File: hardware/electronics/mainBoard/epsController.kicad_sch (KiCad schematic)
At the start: 33 parts, among them SW10 PTS810, SW9 PTS810, U19 STM32L052K8, U20 TCAN3403-Q1

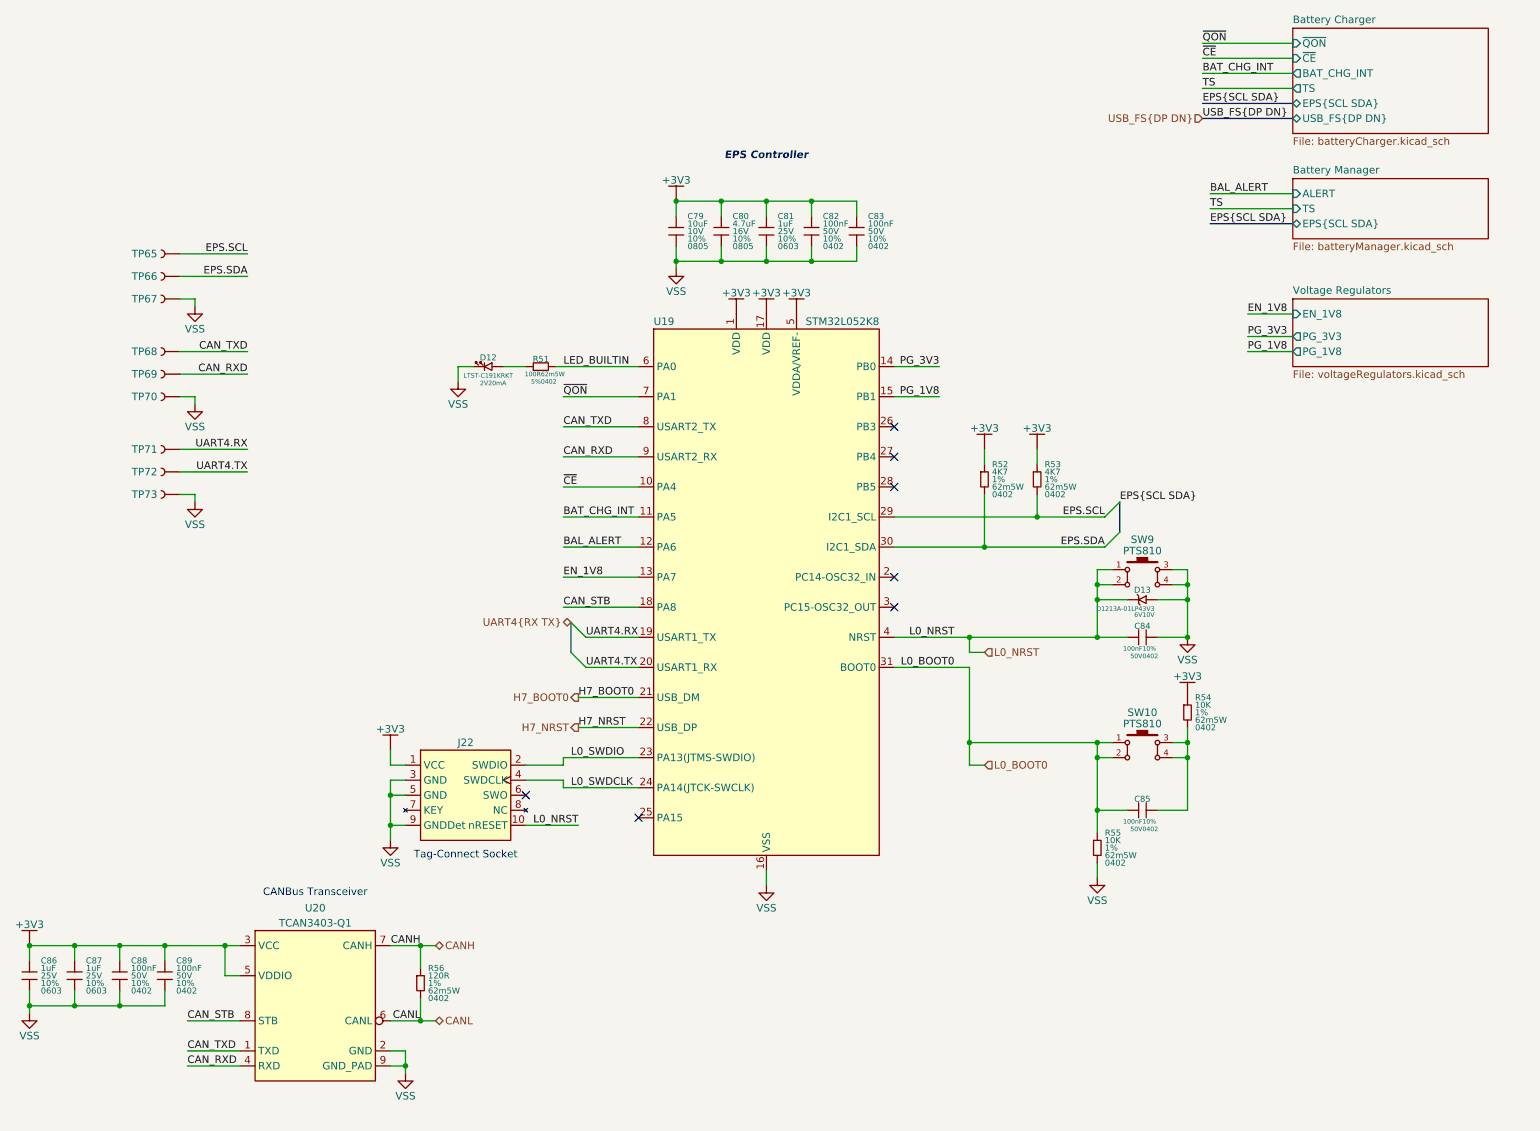
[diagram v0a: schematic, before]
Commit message: updated symbol refs
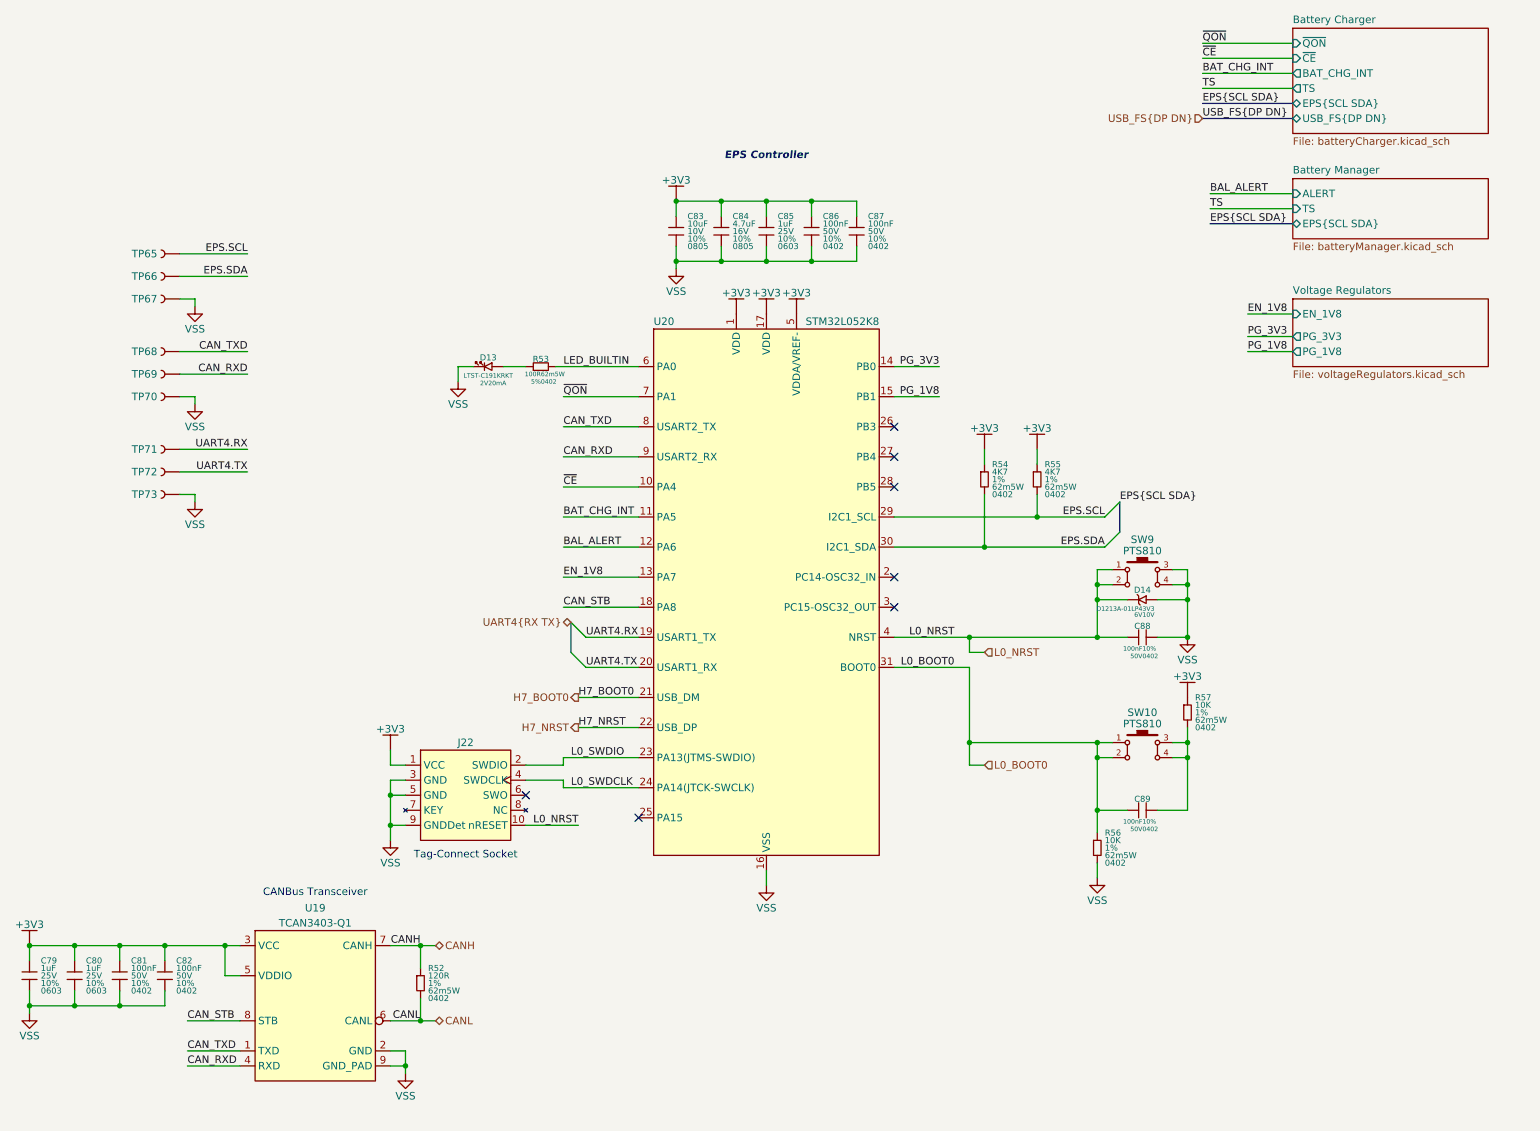
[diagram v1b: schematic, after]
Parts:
- renumbered C86 to C79, C87 to C80, C88 to C81, C89 to C82, C79 to C83, C80 to C84, C81 to C85, C82 to C86, C83 to C87, C84 to C88, C85 to C89, D12 to D13, D13 to D14, R56 to R52, R51 to R53, R52 to R54, R53 to R55, R55 to R56, R54 to R57, U20 to U19, U19 to U20

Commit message: moved CAN transceivers to their own page
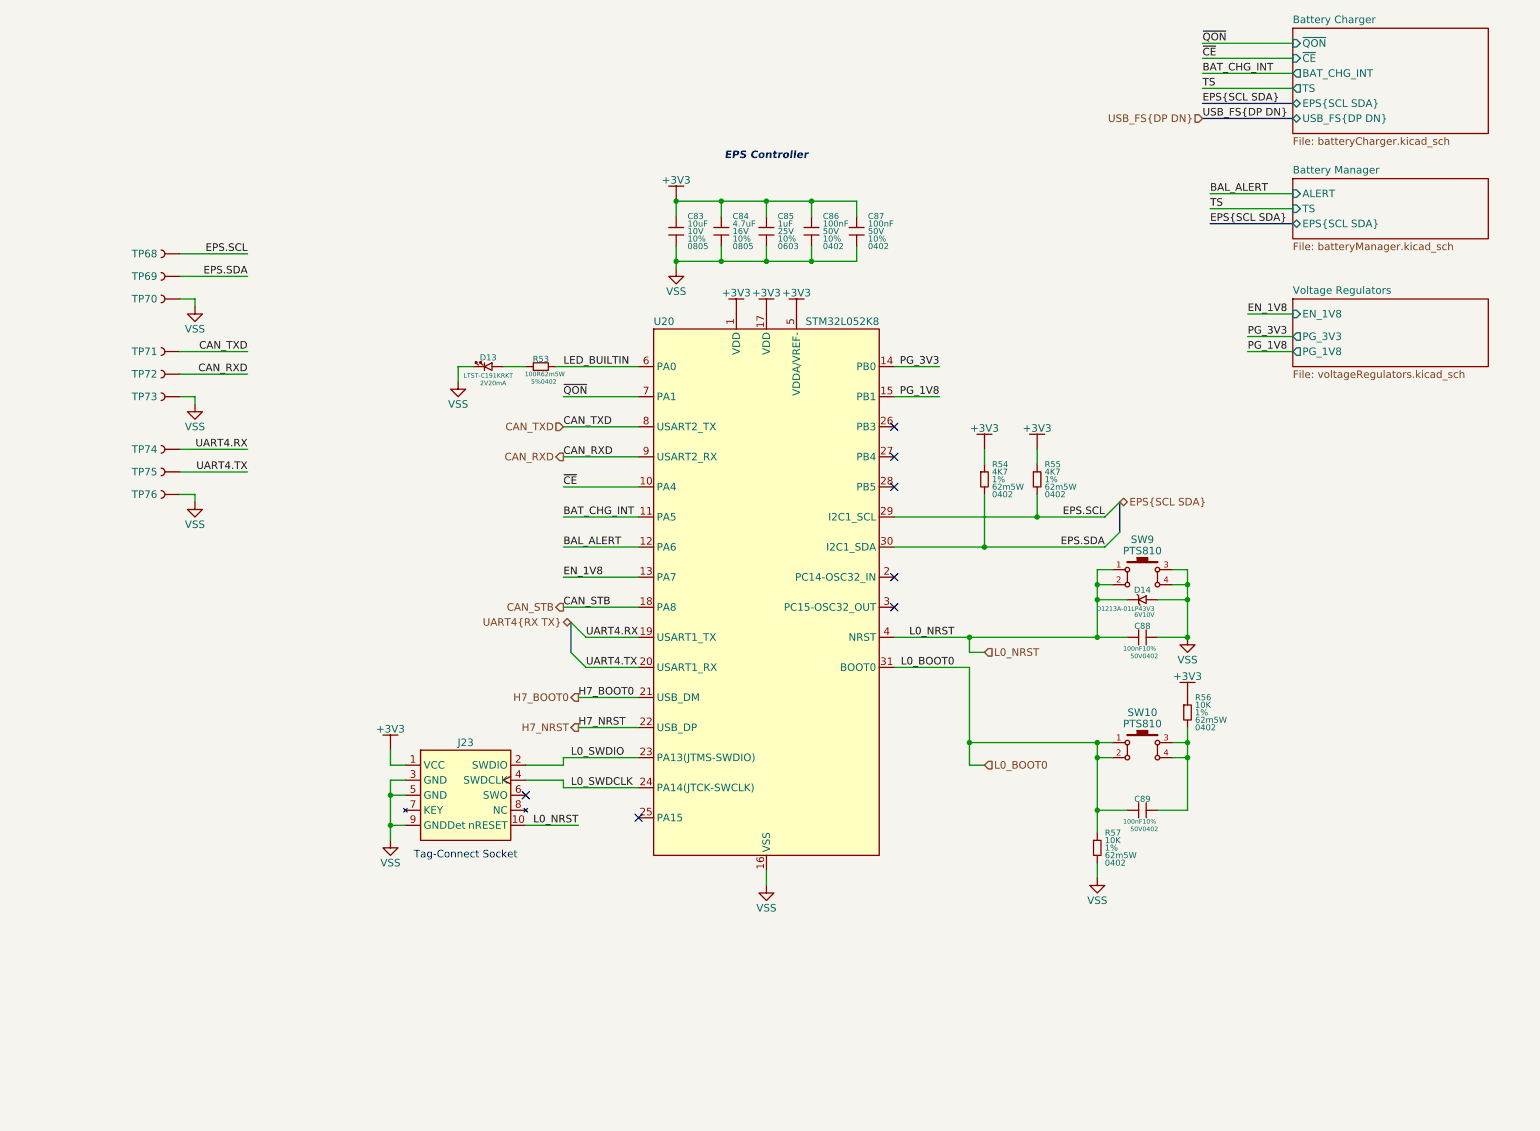
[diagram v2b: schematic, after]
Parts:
- removed C79, C80: 1uF, symbol lib_sch:C
- removed C81, C82: 100nF, symbol lib_sch:C
- removed R52: 120R, symbol lib_sch:R
- removed U19: TCAN3403-Q1, symbol lib_sch:TCAN340x-Q1
- renumbered J22 to J23, R57 to R56, R56 to R57, TP65 to TP68, TP66 to TP69, TP67 to TP70, TP68 to TP71, TP69 to TP72, TP70 to TP73, TP71 to TP74, TP72 to TP75, TP73 to TP76
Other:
- note removed: "CANBus Transceiver"

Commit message: assigned FPs
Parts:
- D14: footprint (none) -> lib_diodes:XDFN2P65_100X60X50L50X25L
- SW10, SW9: footprint (none) -> lib_switches:PTS810
- U20: footprint (none) -> lib_ICs:UFQFPN32
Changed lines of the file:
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@@
 			)
 		)
-		(property "Footprint" ""
+		(property "Footprint" "lib_switches:PTS810"
 			(at 213.995 134.62 0)
 			(effects
@@
 			)
 		)
-		(property "Footprint" ""
+		(property "Footprint" "lib_switches:PTS810"
 			(at 213.995 105.41 0)
 			(effects
@@
 			)
 		)
-		(property "Footprint" ""
+		(property "Footprint" "lib_diodes:XDFN2P65_100X60X50L50X25L"
 			(at 203.835 108.585 0)
 			(effects
@@
 			)
 		)
-		(property "Footprint" ""
+		(property "Footprint" "lib_ICs:UFQFPN32"
 			(at 104.14 95.25 0)
 			(effects

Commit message: added footprints to symbols
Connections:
- net L0_NRST: now also D14.1; no longer D14.2
- net VSS: now also D14.2; no longer D14.1

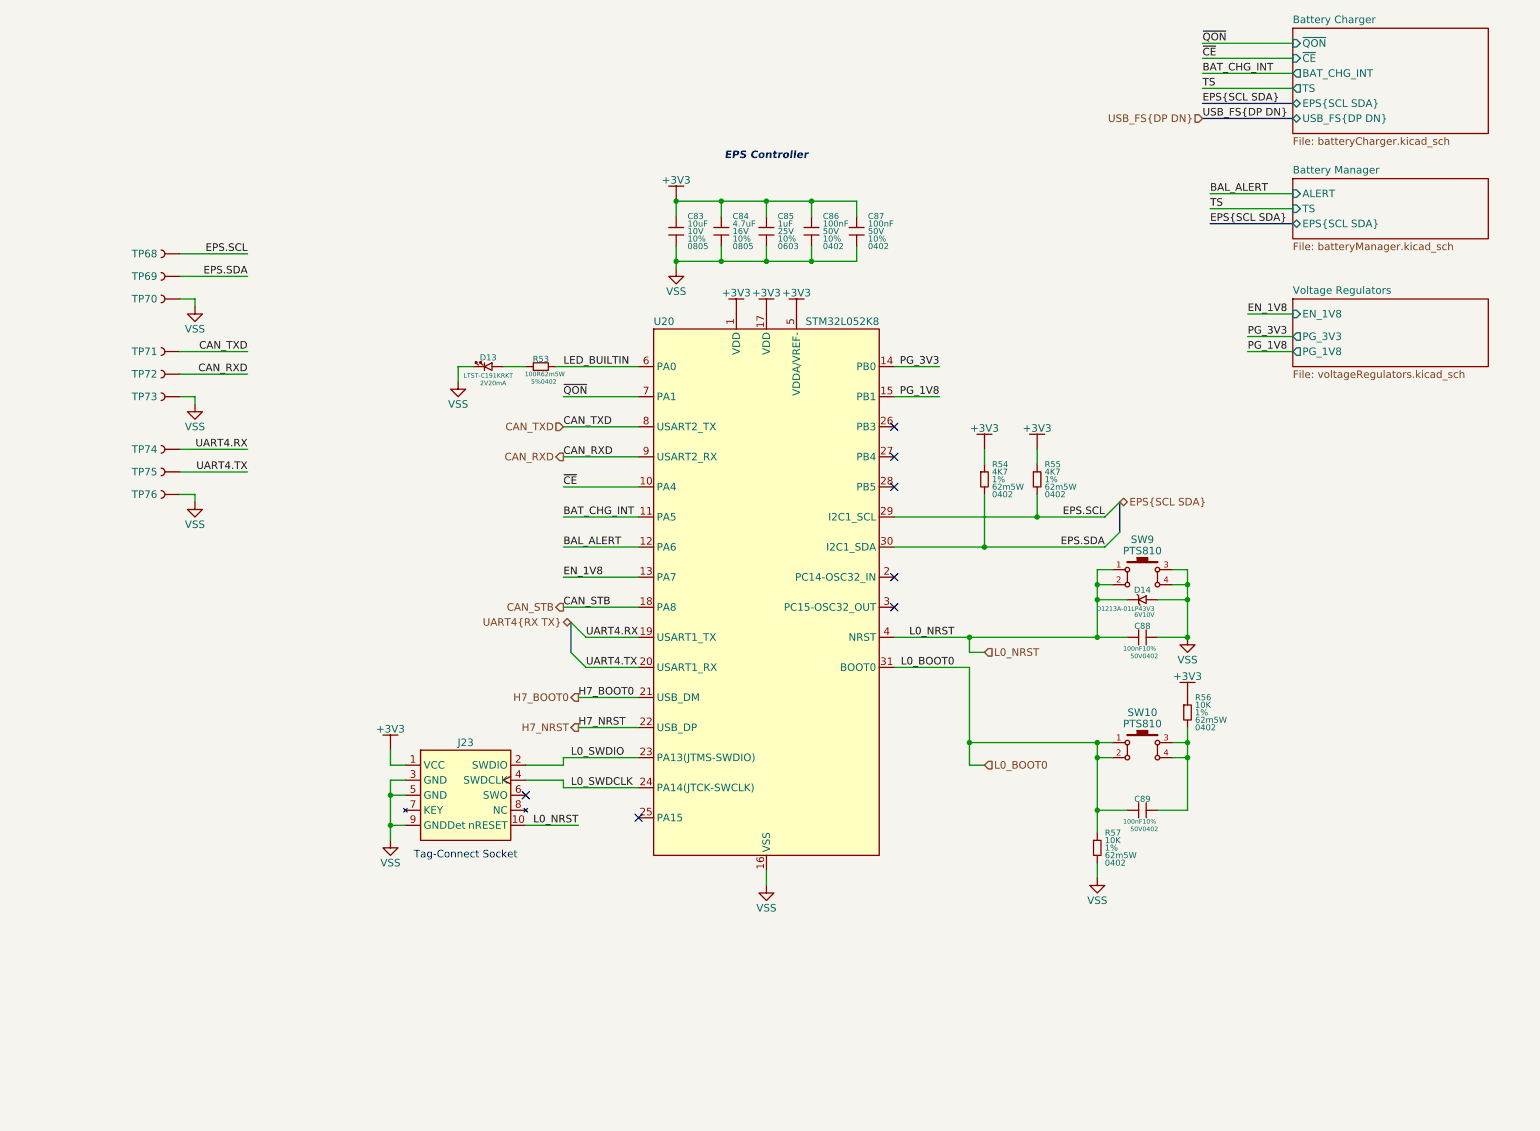
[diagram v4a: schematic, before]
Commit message: assigned footprints
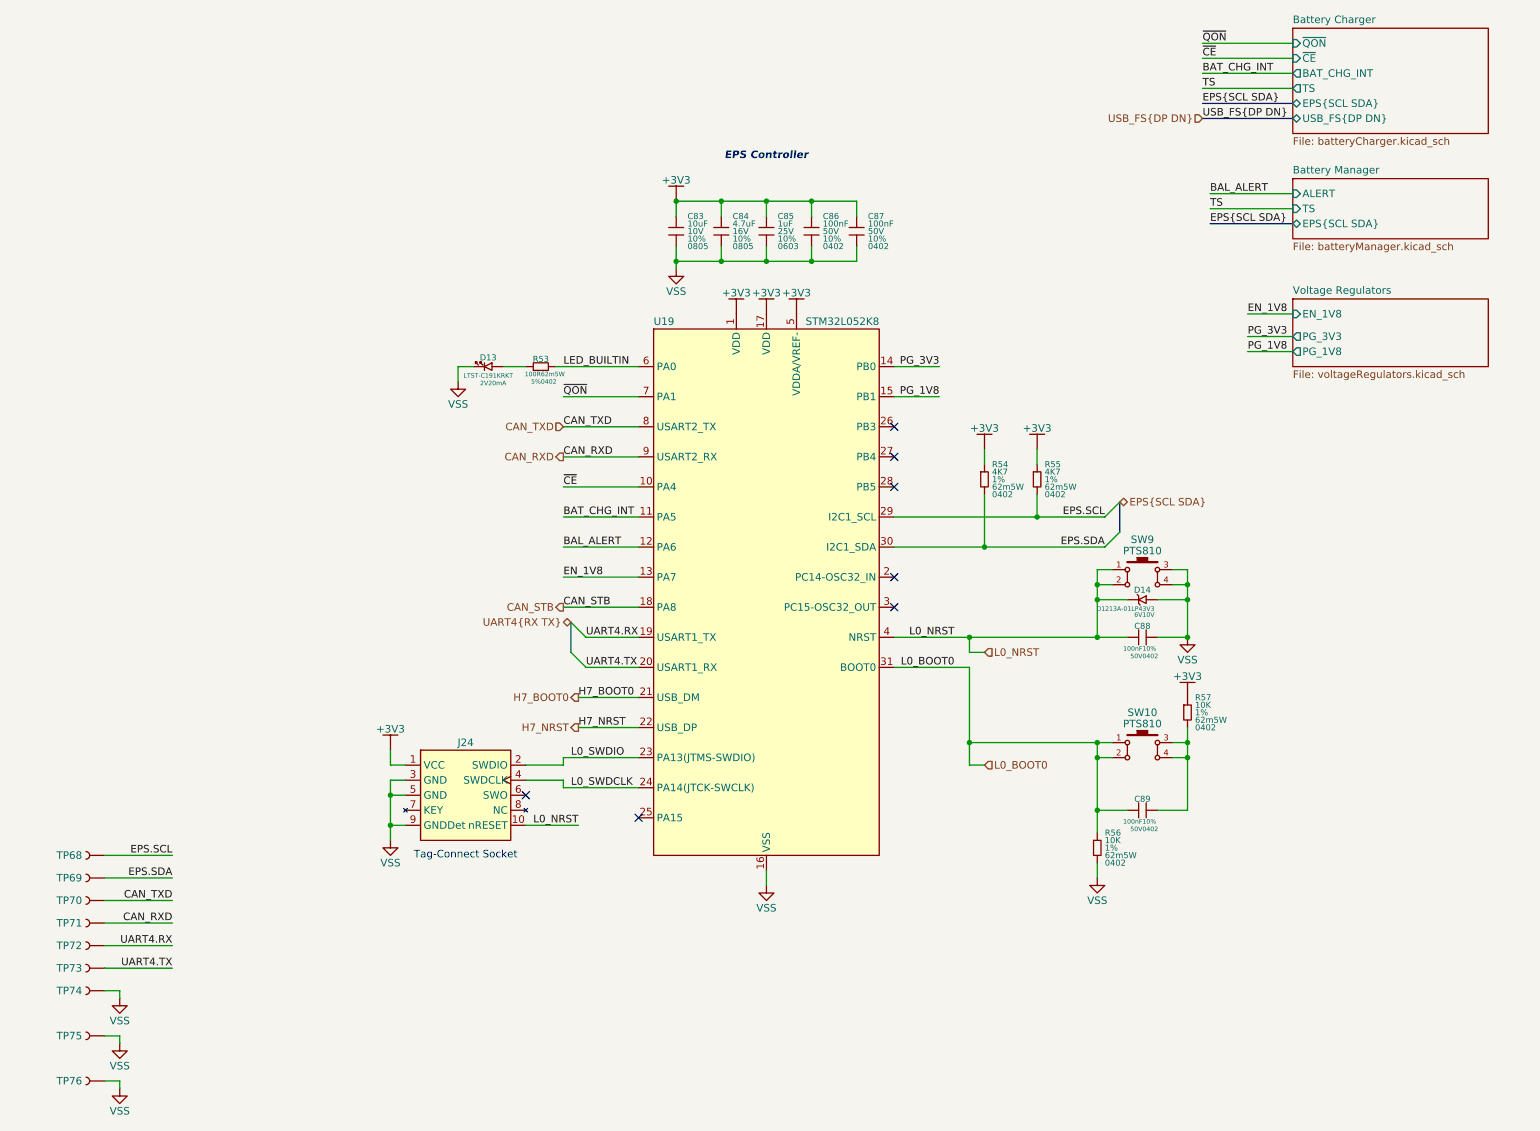
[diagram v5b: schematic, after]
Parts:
- C83, C84: footprint (none) -> lib_passives:GCM0805
- C85: footprint (none) -> lib_passives:GRT0603
- C86, C87, C88, C89: footprint (none) -> lib_passives:GCM0402
- D13: footprint (none) -> lib_diodes:LTST-0603
- J24: renamed from J23; footprint (none) -> lib_misc:TC2050-FP
- R53, R54, R55: footprint (none) -> lib_passives:CRCW0402
- R56: renamed from R57; footprint (none) -> lib_passives:CRCW0402
- R57: renamed from R56; footprint (none) -> lib_passives:CRCW0402
- TP68, TP69: footprint (none) -> lib_misc:TP_2mm
- TP70: renamed from TP71; footprint (none) -> lib_misc:TP_2mm
- TP71: renamed from TP72; footprint (none) -> lib_misc:TP_2mm
- TP72: renamed from TP74; footprint (none) -> lib_misc:TP_2mm
- TP73: renamed from TP75; footprint (none) -> lib_misc:TP_2mm
- TP74: renamed from TP70; footprint (none) -> lib_misc:TP_RCW
- TP75: renamed from TP73; footprint (none) -> lib_misc:TP_RCW
- TP76: footprint (none) -> lib_misc:TP_RCW
- renumbered U20 to U19
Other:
- moved on the sheet: TP68, TP69, TP70, TP71, TP72, TP73, TP74, TP75, TP76
